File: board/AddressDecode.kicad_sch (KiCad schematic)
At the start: 14 parts, among them U16 74LS154, U17 74F541, U19 74F240, U81 ATF22V10C-10PU, U82 ATF22V10C-10PU, U83 ATF22V10C-10PU, U9 74F08

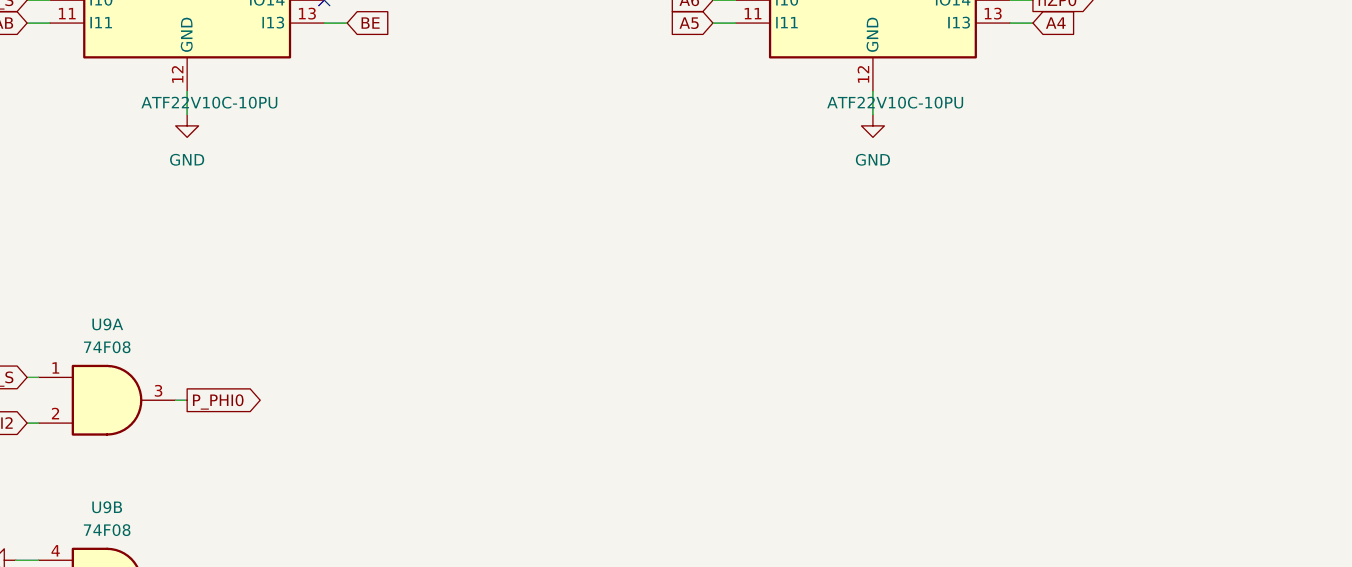
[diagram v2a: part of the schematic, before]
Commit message: V2.0: split Support sheet, add stereo amplifier and on-board speakers
Support sheet reorganized (connectivity unchanged):
- Support.kicad_sch renamed to Power: ATX, front panel, reset, soft power, -5V
- Oscillators and their parts moved to Clocks (now US Ledger)
- Sound-chip decoupling and line-out parts moved to Sound
- VIA CB1/CB2/SPI pull-ups moved to Connectors
- Also includes minor schematic edits made before the reorganization

Audio output rework (Sound, now A3):
- U89 TDA2822M stereo amplifier on 9 V from U90 L7809 (fed by +12V)
- RV1 dual 10k log volume pot behind R26/R27 220k attenuators
- J18 moved from Connectors and now uses the switched TRS symbol:
  a plug lifts T/R off TN/RN and mutes the on-board speakers
- LS1/LS2 8 ohm mini speakers through R30/R31 (15R 0.5 W)
- New footprint Speaker_D32mm_P15.24mm_P17.50mm (two pad pairs, fits
  Adafruit 1898 or Kitronik 3316)
- J39 line-out header (LINE_L, LINE_R, GNDA)
- R18 stays the single GNDA-GND tie, to sit at U89 pin 4
- TDA2822M symbol added to hydra16.kicad_sym

Co-Authored-By: Claude Opus 5.5 <noreply@anthropic.com>
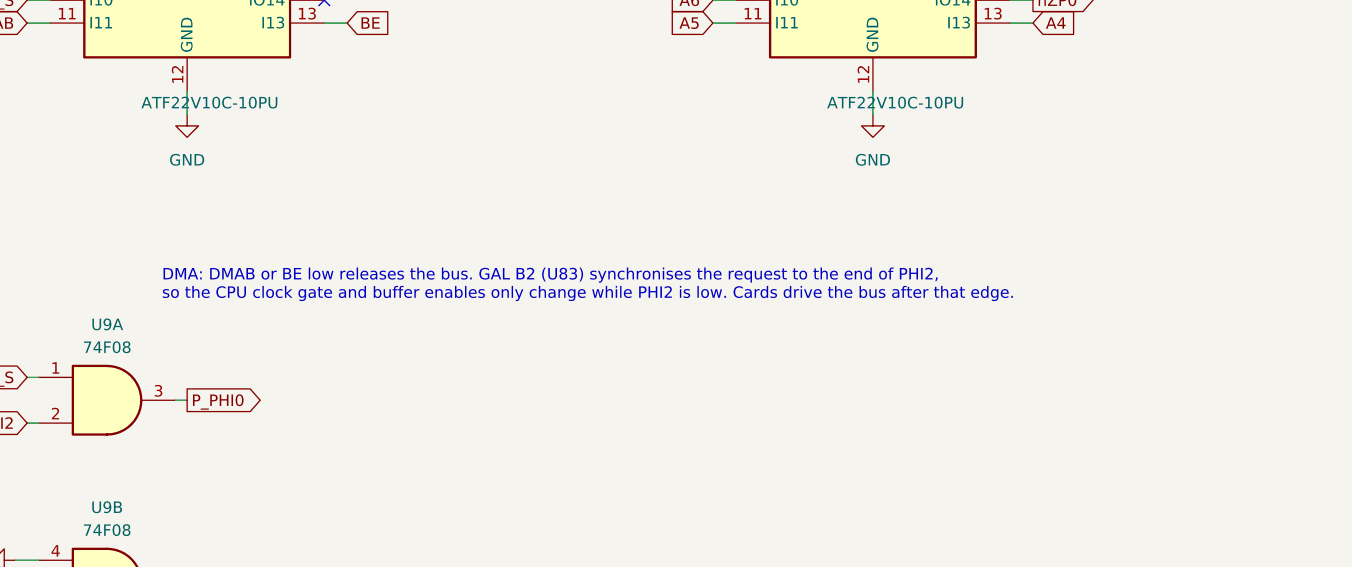
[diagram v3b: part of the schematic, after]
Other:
- note added: "DMA: DMAB or BE low releases the bus. GAL B2 (U83) synchronises the request to the end of PHI2, so the CPU clock gate and buffer enables only change while PHI2 is low. Cards drive the bus after that edge."
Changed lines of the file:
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@@
 	)
 	(no_connect
+		(at 210.82 118.11)
+	)
+	(no_connect
 		(at 146.05 45.72)
 	)
@@
 		(at 269.24 66.04)
 	)
-	(no_connect
-		(at 210.82 118.11)
-	)
 	(bus_entry
 		(at 114.3 48.26)
@@
 	(wire
 		(pts
+			(xy 185.42 118.11) (xy 182.88 118.11)
+		)
+		(stroke
+			(width 0)
+			(type default)
+		)
+	)
+	(wire
+		(pts
 			(xy 43.18 147.32) (xy 43.18 149.86)
 		)
@@
 	(wire
 		(pts
+			(xy 134.62 190.5) (xy 132.08 190.5)
+		)
+		(stroke
+			(width 0)
+			(type default)
+		)
+	)
+	(wire
+		(pts
 			(xy 157.48 128.27) (xy 154.94 128.27)
 		)
@@
 		)
 	)
-	(wire
-		(pts
-			(xy 185.42 118.11) (xy 182.88 118.11)
-		)
-		(stroke
-			(width 0)
-			(type default)
-		)
-	)
-	(wire
-		(pts
-			(xy 134.62 190.5) (xy 132.08 190.5)
-		)
-		(stroke
-			(width 0)
-			(type default)
-		)
-	)
 	(label "A6"
 		(at 118.11 50.8 0)
@@
 		)
 	)
+	(global_label "nIO_S"
+		(shape input)
+		(at 132.08 190.5 180)
+		(fields_autoplaced yes)
+		(effects
+			(font
+				(size 1.27 1.27)
+			)
+			(justify right)
+		)
+		(property "Intersheetrefs" "${INTERSHEET_REFS}"
+			(at 132.08 190.5 180)
+			(effects
+				(font
+					(size 1.27 1.27)
+				)
+				(justify right)
+				(hide yes)
+			)
+		)
+	)
 	(global_label "nBRA_S"
 		(shape input)
@@
 		)
 	)
-	(global_label "nIO_S"
-		(shape input)
-		(at 132.08 190.5 180)
-		(fields_autoplaced yes)
-		(effects
-			(font
-				(size 1.27 1.27)
-			)
-			(justify right)
-		)
-		(property "Intersheetrefs" "${INTERSHEET_REFS}"
-			(at 132.08 190.5 180)
-			(effects
-				(font
-					(size 1.27 1.27)
-				)
-				(justify right)
-				(hide yes)
-			)
-		)
-	)
 	(symbol
 		(lib_id "power:+5V")
@@
 	)
 	(symbol
+		(lib_id "power:GND")
+		(at 182.88 118.11 270)
+		(unit 1)
+		(exclude_from_sim no)
+		(in_bom yes)
+		(on_board yes)
+		(dnp no)
+		(property "Reference" "#PWR2248"
+			(at 182.88 118.11 0)
+			(effects
+				(font
+					(size 1.27 1.27)
+				)
+				(hide yes)
+			)
+		)
+		(property "Value" "GND"
+			(at 177.8 118.11 0)
+			(effects
+				(font
+					(size 1.27 1.27)
+				)
+				(hide yes)
+			)
+		)
+		(property "Footprint" ""
+			(at 182.88 118.11 0)
+			(effects
+				(font
+					(size 1.27 1.27)
+				)
+				(hide yes)
+			)
+		)
+		(property "Datasheet" ""
+			(at 182.88 118.11 0)
+			(effects
+				(font
+					(size 1.27 1.27)
+				)
+				(hide yes)
+			)
+		)
+		(property "Description" "Power symbol creates a global label with name \"GND\""
+			(at 182.88 118.11 0)
+			(effects
+				(font
+					(size 1.27 1.27)
+				)
+				(hide yes)
+			)
+		)
+		(pin "1"
+		)
+		(instances
+			(project "hydra-16"
+				(path "/ef29fc71-3fec-48b5-8a1a-46bee537a98c/e447d2ea-fe27-4cfd-bb5f-eaf105a9519f"
+					(reference "#PWR2248")
+					(unit 1)
+				)
+			)
+		)
+	)
+	(symbol
 		(lib_id "Device:C_Small")
 		(at 73.66 144.78 0)
@@
 		)
 	)
-	(symbol
-		(lib_id "power:GND")
-		(at 182.88 118.11 270)
-		(unit 1)
+	(text "DMA: DMAB or BE low releases the bus. GAL B2 (U83) synchronises the request to the end of PHI2,\nso the CPU clock gate and buffer enables only change while PHI2 is low. Cards drive the bus after that edge."
 		(exclude_from_sim no)
-		(in_bom yes)
-		(on_board yes)
-		(dnp no)
-		(property "Reference" "#PWR2248"
-			(at 182.88 118.11 0)
-			(effects
-				(font
-					(size 1.27 1.27)
-				)
-				(hide yes)
-			)
-		)
-		(property "Value" "GND"
-			(at 177.8 118.11 0)
-			(effects
-				(font
-					(size 1.27 1.27)
-				)
-				(hide yes)
-			)
-		)
-		(property "Footprint" ""
-			(at 182.88 118.11 0)
-			(effects
-				(font
-					(size 1.27 1.27)
-				)
-				(hide yes)
-			)
-		)
-		(property "Datasheet" ""
-			(at 182.88 118.11 0)
-			(effects
-				(font
-					(size 1.27 1.27)
-				)
-				(hide yes)
-			)
-		)
-		(property "Description" "Power symbol creates a global label with name \"GND\""
-			(at 182.88 118.11 0)
-			(effects
-				(font
-					(size 1.27 1.27)
-				)
-				(hide yes)
-			)
-		)
-		(pin "1"
-		)
-		(instances
-			(project "hydra-16"
-				(path "/ef29fc71-3fec-48b5-8a1a-46bee537a98c/e447d2ea-fe27-4cfd-bb5f-eaf105a9519f"
-					(reference "#PWR2248")
-					(unit 1)
-				)
+		(at 251.206 101.064 0)
+		(effects
+			(font
+				(size 1.27 1.27)
 			)
+			(justify left top)
 		)
 	)

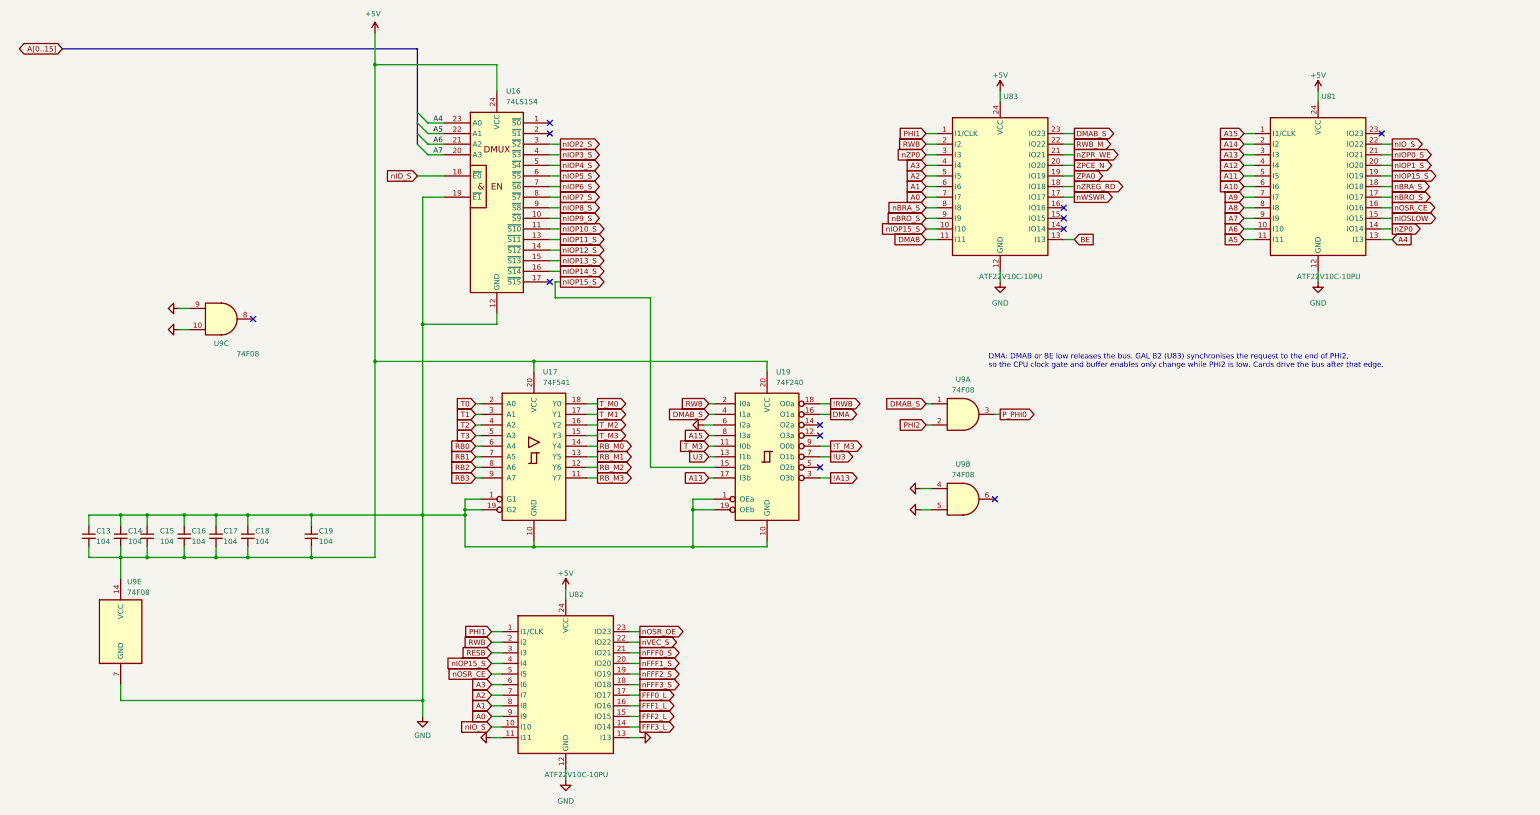
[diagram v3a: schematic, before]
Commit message: V2.0: consolidate parts (239 -> 216), GAL C rev 02
No change in function:
- U9 74F08 removed: GAL C (U88) rev 02 makes the CPU phi0 (P_PHI0 = PHI2
  held low while DMAB_S is low); its decoupling cap C14 removed
- U34 74ACT14 removed: the two clock buffers use spare U19 74F240 gates
- U60 + U61 (2 x CY7C192 vector RAM) replaced by one AS7C256B-15
  (32K x 8, 15 ns); the IRQ sheet's D[0..7] bus is gone
- Crystal oscillators (U75 74HCU04, Y1, Y2, R1, R6-R8, C43, C44, C96,
  C97) replaced by canned oscillators X1 (14.31818 MHz), X2 (1.8432 MHz)
- Soft power: CD40106 -> 74HC14, CD4013 -> 74HC74 (active-low set/reset,
  power-on reset network inverted); a spare 74HC14 gate drives PS_ON#,
  so Q1 is removed
- R10-R13 -> RN6 (4 x 10k, SIP-5); R9, R21-R24 -> RN7 (5 x 33R isolated,
  SIP-10)
- C100-C102 (3 x 220u) -> C100 680u
- Clocks and Power sheet notes updated; PLD README updated

GAL C rev 02 verified against rev 01 over 200,000 clock edges.
PCB updated from the schematic (adds RN6, RN7, X1, X2 and the speakers
LS1/LS2). Also includes KiCad's re-save of the schematic sheets.

Co-Authored-By: Claude Opus 5.5 <noreply@anthropic.com>
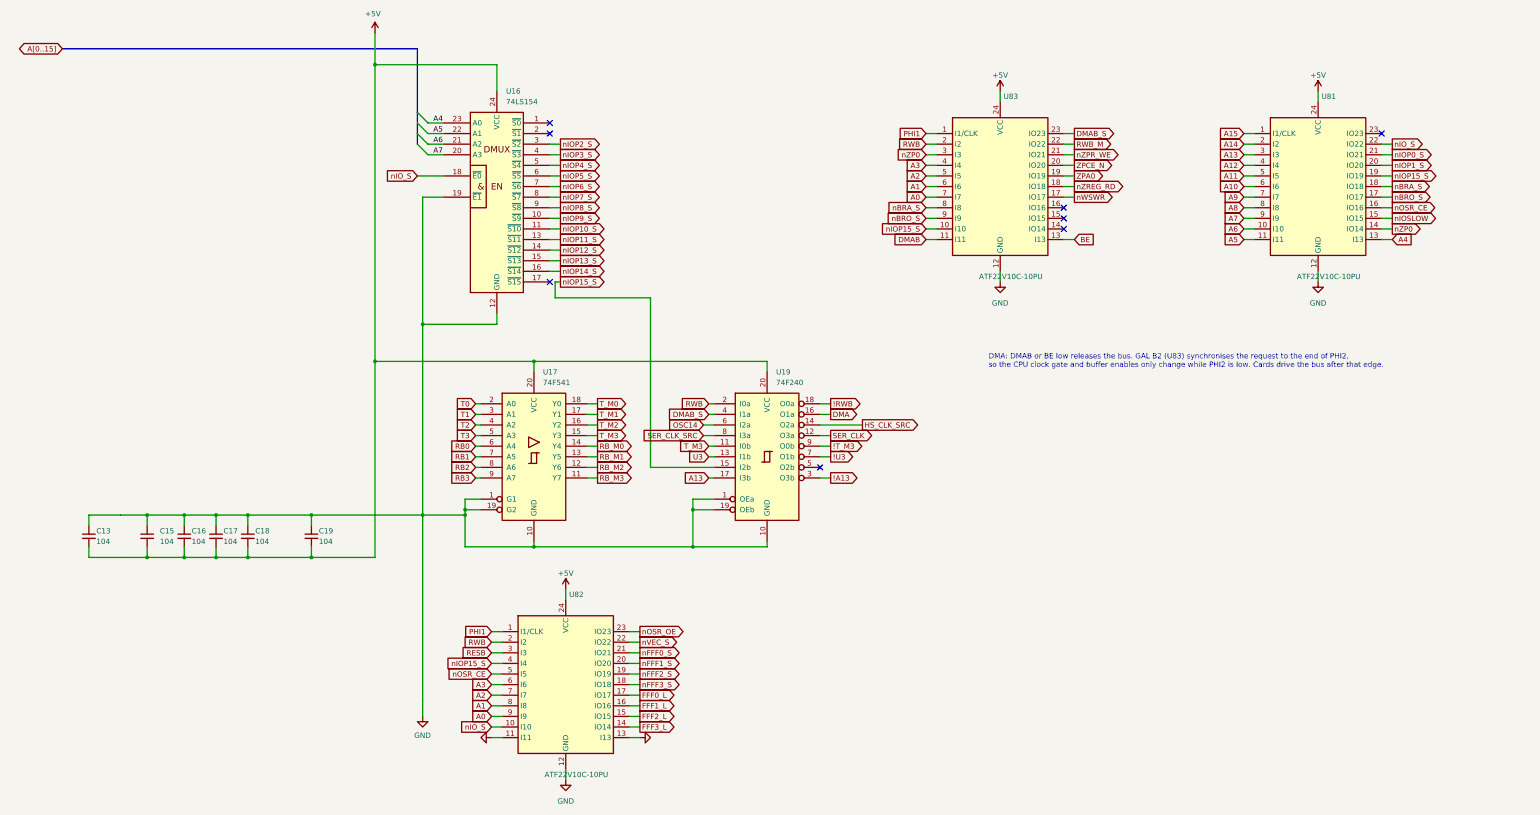
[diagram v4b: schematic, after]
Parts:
- removed C14: 104, Capacitor_THT:C_Disc_D5.0mm_W2.5mm_P5.00mm, symbol Device:C_Small
- removed U9: 74F08, Package_DIP:DIP-14_W7.62mm_Socket_LongPads, symbol 74xx:74LS08
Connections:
- net A15: no longer U19.8 (I3a)
- net GND: no longer U19.6 (I2a)
- net SER_CLK: now reaches U19.12 (O3a)
- net HS_CLK_SRC: now reaches U19.14 (O2a)
- new net OSC14: U19.6 (I2a)
- new net SER_CLK_SRC: U19.8 (I3a)
- no-connect marks 12 -> 8
